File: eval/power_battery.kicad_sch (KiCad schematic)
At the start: 52 parts, among them Q10 2N7002, Q9 2N7002, U18 TLV3501AIDBV, U20 LM2903, U22 SN74LVC1G00DBV, U23 SN74LVC1G00DBV, U24 HYG015N03LS1C2, U25 HYG015N03LS1C2, U7 MX74502D23_C41433189

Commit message: [layout] layout completed, ready for trace
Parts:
- added JP1, JP2, JP3, JP4: SolderJumper_2_Bridged, Jumper:SolderJumper-2_P1.3mm_Bridged_RoundedPad1.0x1.5mm, symbol Jumper:SolderJumper_2_Bridged
- TP1, TP2, TP4, TP5, TP6, TP7, TP8, TP9: footprint (none) -> TestPoint:TestPoint_Pad_D2.0mm
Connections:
- net OV: now also JP1.2 (B); no longer C53.1, D5.1 (K), R50.1
- net power_on_hold: now also JP2.2 (B), JP3.2 (B), JP4.2 (B); no longer Q9.3 (D), TP1.1, TP2.1, U20.1, U20.7
- new net: C53.1, D5.1 (K), JP1.1 (A), R50.1
- new net: JP4.1 (A), Q9.3 (D)
- new net: JP3.1 (A), TP2.1, U20.7
- new net: JP2.1 (A), TP1.1, U20.1

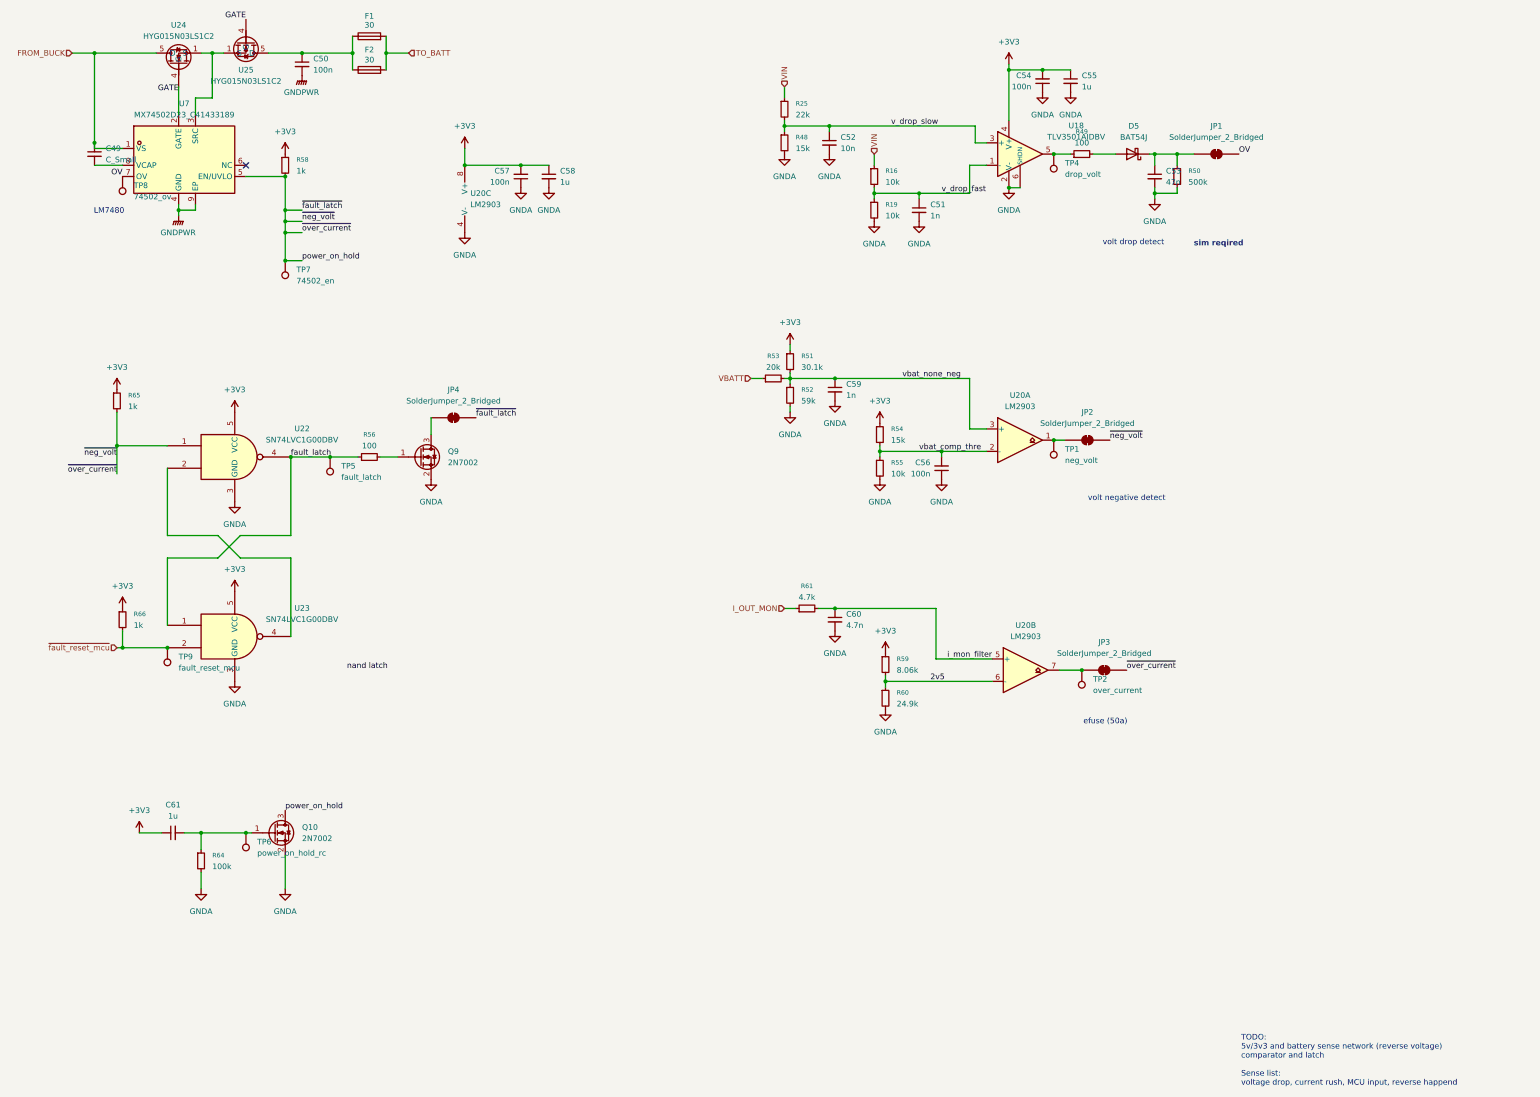
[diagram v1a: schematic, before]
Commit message: [trace] add high power trace
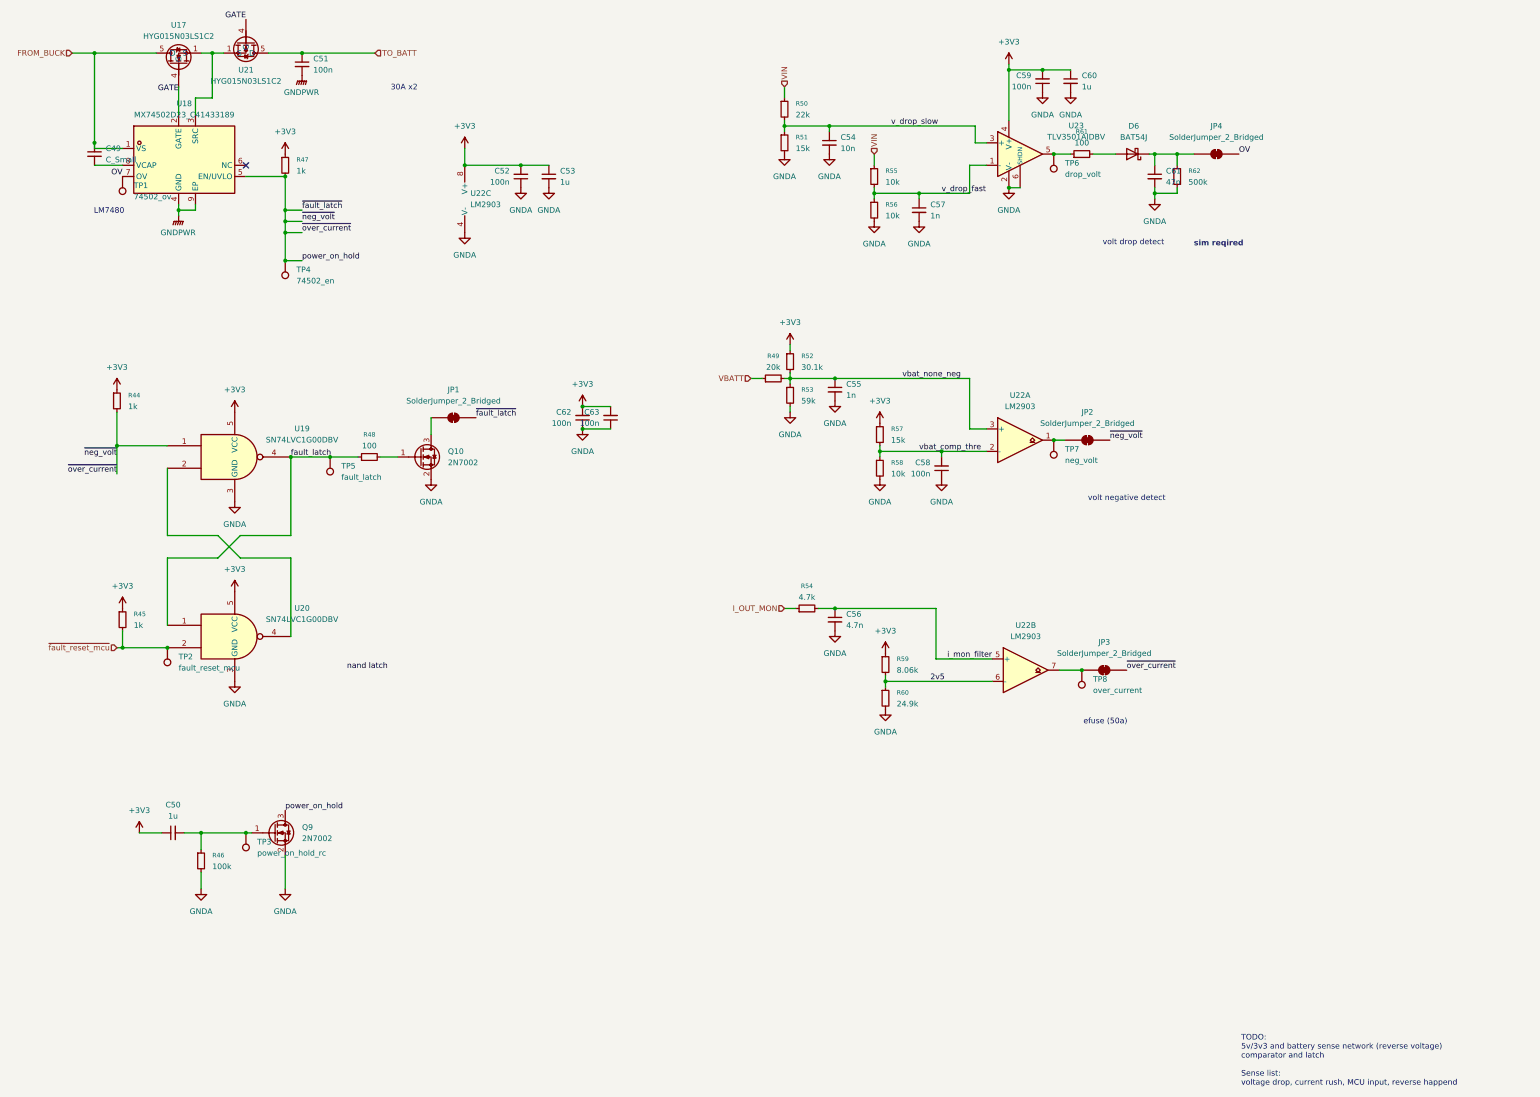
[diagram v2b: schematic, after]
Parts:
- removed F1, F2: 30, symbol Device:Fuse
- added C62, C63: 100n, Capacitor_SMD:C_0603_1608Metric, symbol Device:C_Small
- renumbered C61 to C50, C50 to C51, C57 to C52, C58 to C53, C52 to C54, C59 to C55, C60 to C56, C51 to C57, C56 to C58, C54 to C59, C55 to C60, C53 to C61, D5 to D6, JP4 to JP1, JP1 to JP4, Q9 to Q10, Q10 to Q9, R65 to R44, R66 to R45, R64 to R46, R58 to R47, R56 to R48, R53 to R49, R25 to R50, R48 to R51, R51 to R52, R52 to R53, R61 to R54, R16 to R55, R19 to R56, R54 to R57, R55 to R58, R49 to R61, R50 to R62, TP8 to TP1, TP9 to TP2, TP6 to TP3, TP7 to TP4, TP4 to TP6, TP1 to TP7, TP2 to TP8, U24 to U17, U7 to U18, U22 to U19, U23 to U20, U25 to U21, U20 to U22, U18 to U23
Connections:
- net +3V3: now also C62.2, C63.2
- net GNDA: now also C62.1, C63.1
- net TO_BATT: now also C51.1, U21.5 (D), U21.6 (D), U21.7 (D), U21.8 (D), U21.9 (D)
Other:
- note added: "30A x2"

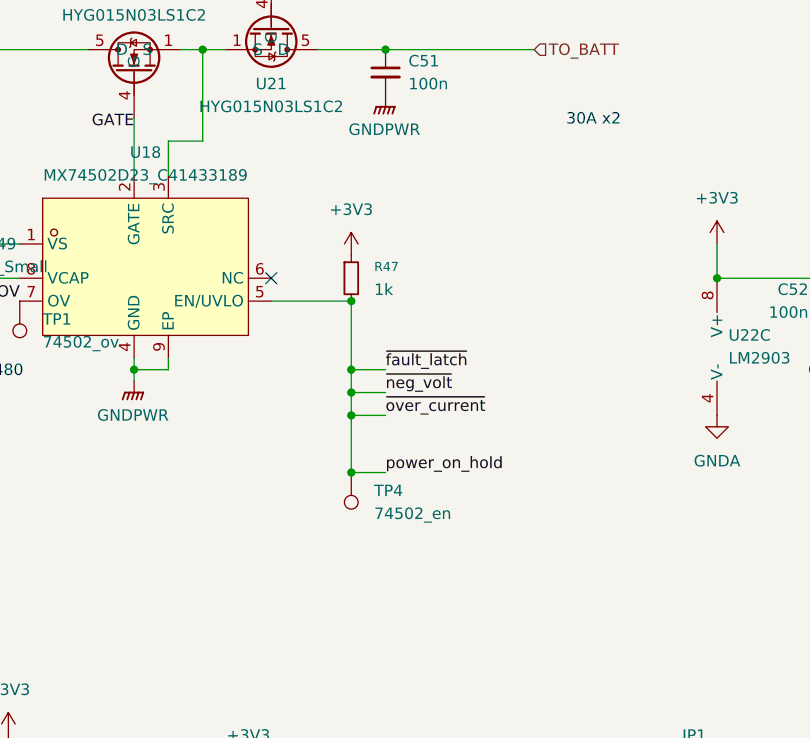
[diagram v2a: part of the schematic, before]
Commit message: [trace] Add USB trace (with impedance control)
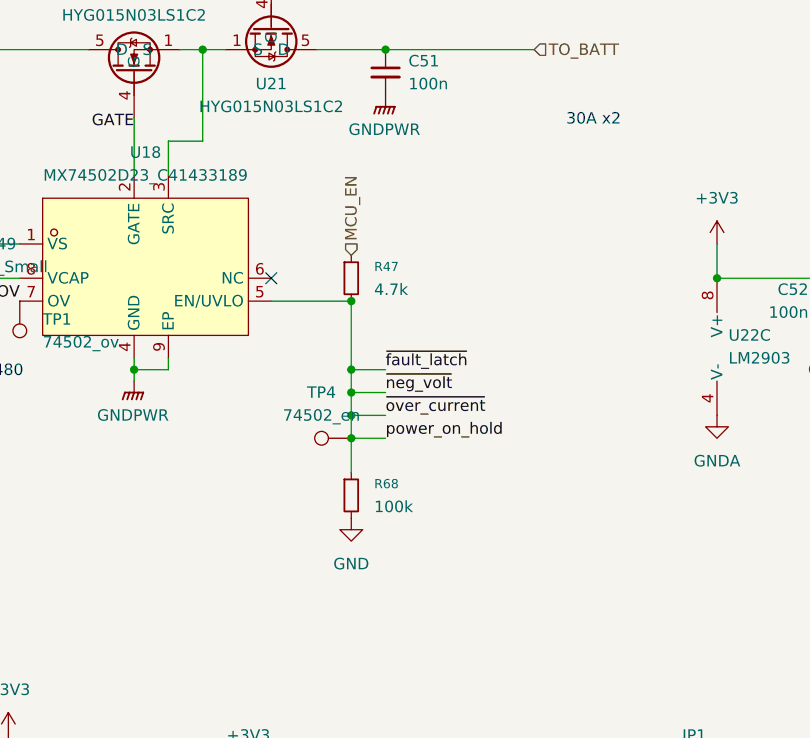
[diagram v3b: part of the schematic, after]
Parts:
- added R68: 100k, Resistor_SMD:R_0603_1608Metric, symbol Device:R_Small
- R47: value 1k -> 4.7k
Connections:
- net +3V3: no longer R47.1
- net power_on_hold: now also R68.1
- new net GND: R68.2
- new net MCU_EN: R47.1
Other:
- moved on the sheet: TP4
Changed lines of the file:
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@@
 	)
 	(junction
-		(at 87.63 80.01)
-		(diameter 0)
-		(color 0 0 0 0)
-	)
-	(junction
 		(at 261.62 55.88)
 		(diameter 0)
@@
 	)
 	(junction
+		(at 87.63 76.2)
+		(diameter 0)
+		(color 0 0 0 0)
+	)
+	(junction
 		(at 259.08 36.83)
 		(diameter 0)
@@
 	(wire
 		(pts
-			(xy 91.44 80.01) (xy 87.63 80.01)
+			(xy 91.44 76.2) (xy 87.63 76.2)
 		)
 		(stroke
@@
 	(wire
 		(pts
-			(xy 87.63 73.66) (xy 87.63 80.01)
+			(xy 87.63 73.66) (xy 87.63 76.2)
 		)
 		(stroke
@@
 	(wire
 		(pts
+			(xy 87.63 76.2) (xy 87.63 80.01)
+		)
+		(stroke
+			(width 0)
+			(type default)
+		)
+	)
+	(wire
+		(pts
 			(xy 203.2 158.75) (xy 200.66 158.75)
 		)
@@
 	)
 	(label "power_on_hold"
-		(at 91.44 80.01 0)
+		(at 91.44 76.2 0)
 		(effects
 			(font
@@
 		)
 	)
+	(hierarchical_label "MCU_EN"
+		(shape input)
+		(at 87.63 55.88 90)
+		(effects
+			(font
+				(size 1.27 1.27)
+			)
+			(justify left)
+		)
+	)
 	(hierarchical_label "I_OUT_MON"
 		(shape input)
@@
 			)
 		)
-		(property "Value" "1k"
+		(property "Value" "4.7k"
 			(at 90.17 59.6899 0)
 			(show_name no)
@@
 	)
 	(symbol
+		(lib_id "power:GND")
+		(at 87.63 85.09 0)
+		(unit 1)
+		(body_style 1)
+		(exclude_from_sim no)
+		(in_bom yes)
+		(on_board yes)
+		(in_pos_files yes)
+		(dnp no)
+		(fields_autoplaced yes)
+		(property "Reference" "#PWR030"
+			(at 87.63 91.44 0)
+			(hide yes)
+			(show_name no)
+			(do_not_autoplace no)
+			(effects
+				(font
+					(size 1.27 1.27)
+				)
+			)
+		)
+		(property "Value" "GND"
+			(at 87.63 90.17 0)
+			(show_name no)
+			(do_not_autoplace no)
+			(effects
+				(font
+					(size 1.27 1.27)
+				)
+			)
+		)
+		(property "Footprint" ""
+			(at 87.63 85.09 0)
+			(hide yes)
+			(show_name no)
+			(do_not_autoplace no)
+			(effects
+				(font
+					(size 1.27 1.27)
+				)
+			)
+		)
+		(property "Datasheet" ""
+			(at 87.63 85.09 0)
+			(hide yes)
+			(show_name no)
+			(do_not_autoplace no)
+			(effects
+				(font
+					(size 1.27 1.27)
+				)
+			)
+		)
+		(property "Description" "Power symbol creates a global label with name \"GND\" , ground"
+			(at 87.63 85.09 0)
+			(hide yes)
+			(show_name no)
+			(do_not_autoplace no)
+			(effects
+				(font
+					(size 1.27 1.27)
+				)
+			)
+		)
+		(pin "1"
+		)
+		(instances
+			(project "eval"
+				(path "/8b023652-20db-48ce-ad53-bc2d9a4e5dd4/4380f3ef-c4d9-44b0-bf49-4e0cf7323e12"
+					(reference "#PWR030")
+					(unit 1)
+				)
+			)
+		)
+	)
+	(symbol
 		(lib_id "Device:C_Small")
 		(at 284.48 60.96 0)
@@
 	)
 	(symbol
+		(lib_id "Device:R_Small")
+		(at 87.63 82.55 0)
+		(unit 1)
+		(body_style 1)
+		(exclude_from_sim no)
+		(in_bom yes)
+		(on_board yes)
+		(in_pos_files yes)
+		(dnp no)
+		(fields_autoplaced yes)
+		(property "Reference" "R68"
+			(at 90.17 81.2799 0)
+			(show_name no)
+			(do_not_autoplace no)
+			(effects
+				(font
+					(size 1.016 1.016)
+				)
+				(justify left)
+			)
+		)
+		(property "Value" "100k"
+			(at 90.17 83.8199 0)
+			(show_name no)
+			(do_not_autoplace no)
+			(effects
+				(font
+					(size 1.27 1.27)
+				)
+				(justify left)
+			)
+		)
+		(property "Footprint" "Resistor_SMD:R_0603_1608Metric"
+			(at 87.63 82.55 0)
+			(hide yes)
+			(show_name no)
+			(do_not_autoplace no)
+			(effects
+				(font
+					(size 1.27 1.27)
+				)
+			)
+		)
+		(property "Datasheet" ""
+			(at 87.63 82.55 0)
+			(hide yes)
+			(show_name no)
+			(do_not_autoplace no)
+			(effects
+				(font
+					(size 1.27 1.27)
+				)
+			)
+		)
+		(property "Description" "Resistor, small symbol"
+			(at 87.63 82.55 0)
+			(hide yes)
+			(show_name no)
+			(do_not_autoplace no)
+			(effects
+				(font
+					(size 1.27 1.27)
+				)
+			)
+		)
+		(pin "2"
+		)
+		(pin "1"
+		)
+		(instances
+			(project "eval"
+				(path "/8b023652-20db-48ce-ad53-bc2d9a4e5dd4/4380f3ef-c4d9-44b0-bf49-4e0cf7323e12"
+					(reference "R68")
+					(unit 1)
+				)
+			)
+		)
+	)
+	(symbol
 		(lib_id "power:+3V3")
 		(at 154.94 113.03 0)
@@
 	)
 	(symbol
-		(lib_id "power:+3V3")
-		(at 87.63 55.88 0)
-		(unit 1)
-		(body_style 1)
-		(exclude_from_sim no)
-		(in_bom yes)
-		(on_board yes)
-		(in_pos_files yes)
-		(dnp no)
-		(fields_autoplaced yes)
-		(property "Reference" "#PWR0112"
-			(at 87.63 59.69 0)
-			(hide yes)
-			(show_name no)
-			(do_not_autoplace no)
-			(effects
-				(font
-					(size 1.27 1.27)
-				)
-			)
-		)
-		(property "Value" "+3V3"
-			(at 87.63 50.8 0)
-			(show_name no)
-			(do_not_autoplace no)
-			(effects
-				(font
-					(size 1.27 1.27)
-				)
-			)
-		)
-		(property "Footprint" ""
-			(at 87.63 55.88 0)
-			(hide yes)
-			(show_name no)
-			(do_not_autoplace no)
-			(effects
-				(font
-					(size 1.27 1.27)
-				)
-			)
-		)
-		(property "Datasheet" ""
-			(at 87.63 55.88 0)
-			(hide yes)
-			(show_name no)
-			(do_not_autoplace no)
-			(effects
-				(font
-					(size 1.27 1.27)
-				)
-			)
-		)
-		(property "Description" "Power symbol creates a global label with name \"+3V3\""
-			(at 87.63 55.88 0)
-			(hide yes)
-			(show_name no)
-			(do_not_autoplace no)
-			(effects
-				(font
-					(size 1.27 1.27)
-				)
-			)
-		)
-		(pin "1"
-		)
-		(instances
-			(project "eval"
-				(path "/8b023652-20db-48ce-ad53-bc2d9a4e5dd4/4380f3ef-c4d9-44b0-bf49-4e0cf7323e12"
-					(reference "#PWR0112")
-					(unit 1)
-				)
-			)
-		)
-	)
-	(symbol
 		(lib_id "Device:R_Small")
 		(at 220.98 60.96 0)
@@
 	(symbol
 		(lib_id "Connector:TestPoint")
-		(at 87.63 80.01 180)
+		(at 87.63 76.2 90)
 		(unit 1)
 		(body_style 1)
@@
 		(fields_autoplaced yes)
 		(property "Reference" "TP4"
-			(at 90.17 82.0419 0)
+			(at 84.328 71.12 90)
 			(show_name no)
 			(do_not_autoplace no)
@@
 					(size 1.27 1.27)
 				)
-				(justify right)
 			)
 		)
 		(property "Value" "74502_en"
-			(at 90.17 84.5819 0)
+			(at 84.328 73.66 90)
 			(show_name no)
 			(do_not_autoplace no)
@@
 					(size 1.27 1.27)
 				)
-				(justify right)
 			)
 		)
 		(property "Footprint" "TestPoint:TestPoint_Pad_D2.0mm"
-			(at 82.55 80.01 0)
+			(at 87.63 71.12 0)
 			(hide yes)
 			(show_name no)
@@
 		)
 		(property "Datasheet" ""
-			(at 82.55 80.01 0)
+			(at 87.63 71.12 0)
 			(hide yes)
 			(show_name no)
@@
 		)
 		(property "Description" "test point"
-			(at 87.63 80.01 0)
+			(at 87.63 76.2 0)
 			(hide yes)
 			(show_name no)
